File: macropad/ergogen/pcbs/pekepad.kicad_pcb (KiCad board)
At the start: 2 copper layers, 196 x 43.9 mm, 37 parts

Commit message: More case fixes
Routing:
- net P024: track 0.00 -> 183.9 mm, vias 0 -> 2
- net P008: track 0.00 -> 102.9 mm, vias 0 -> 1
- net P031: track 0.00 -> 101.5 mm, vias 0 -> 2
- net P106: track 0.00 -> 86.1 mm
- net P111: track 0.00 -> 85.7 mm
- net P022: track 0.00 -> 82.1 mm, vias 0 -> 2
- net P104: track 0.00 -> 81.7 mm
- net P009: track 0.00 -> 81.1 mm
- net P115: track 0.00 -> 71.9 mm, vias 0 -> 2
- net P113: track 0.00 -> 68.1 mm
- net P017: track 0.00 -> 66.6 mm, vias 0 -> 1
- net P100: track 0.00 -> 64.4 mm
- net P020: track 0.00 -> 52.7 mm, vias 0 -> 1
- net P029: track 0.00 -> 52.1 mm, vias 0 -> 1
- net P006: track 0.00 -> 44.7 mm
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
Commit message: More fixes to the case/pcb/plate
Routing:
- net P024: track 183.9 -> 0.00 mm, vias 2 -> 0
- net P008: track 102.9 -> 0.00 mm, vias 1 -> 0
- net P031: track 101.5 -> 0.00 mm, vias 2 -> 0
- net P106: track 86.1 -> 0.00 mm
- net P111: track 85.7 -> 0.00 mm
- net P022: track 82.1 -> 0.00 mm, vias 2 -> 0
- net P104: track 81.7 -> 0.00 mm
- net P009: track 81.1 -> 0.00 mm
- net P115: track 71.9 -> 0.00 mm, vias 2 -> 0
- net P113: track 68.1 -> 0.00 mm
- net P017: track 66.6 -> 0.00 mm, vias 1 -> 0
- net P100: track 64.4 -> 0.00 mm
- net P020: track 52.7 -> 0.00 mm, vias 1 -> 0
- net P029: track 52.1 -> 0.00 mm, vias 1 -> 0
- net P006: track 44.7 -> 0.00 mm
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
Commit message: forgot pcb wiring
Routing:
- net P024: track 0.00 -> 179.0 mm, vias 0 -> 2
- net P031: track 0.00 -> 103.2 mm, vias 0 -> 1
- net P008: track 0.00 -> 101.0 mm, vias 0 -> 1
- net P106: track 0.00 -> 86.1 mm
- net P111: track 0.00 -> 85.6 mm
- net P104: track 0.00 -> 81.7 mm
- net P009: track 0.00 -> 81.1 mm
- net P115: track 0.00 -> 73.6 mm, vias 0 -> 3
- net P113: track 0.00 -> 68.1 mm
- net P017: track 0.00 -> 66.6 mm, vias 0 -> 1
- net P100: track 0.00 -> 64.1 mm
- net P022: track 0.00 -> 59.7 mm, vias 0 -> 2
- net P029: track 0.00 -> 51.9 mm, vias 0 -> 1
- net P020: track 0.00 -> 46.8 mm, vias 0 -> 2
- net P006: track 0.00 -> 44.7 mm
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
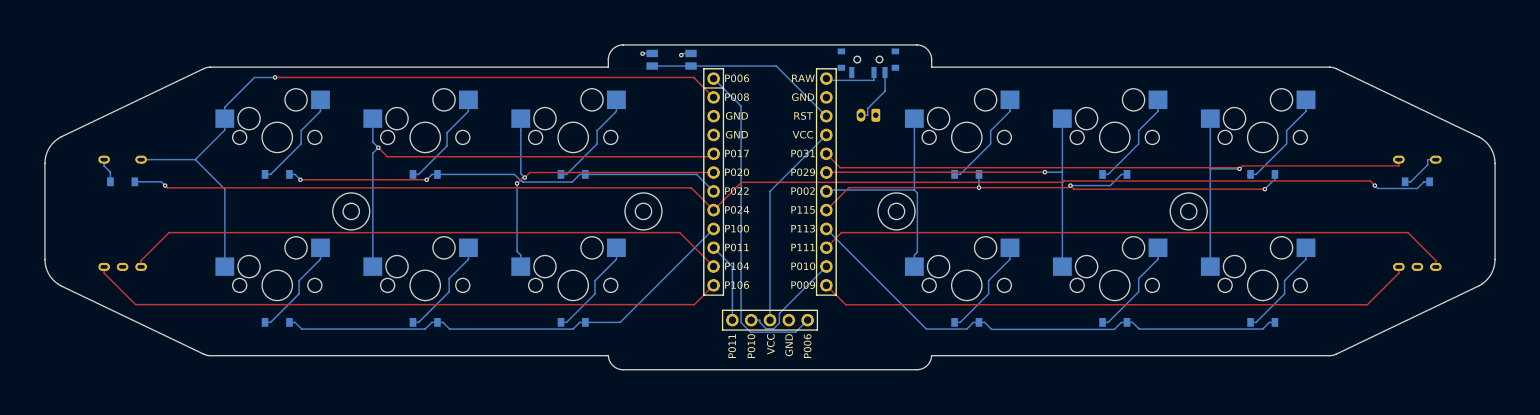
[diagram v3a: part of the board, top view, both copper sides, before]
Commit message: adjusting I2C/SPI pins
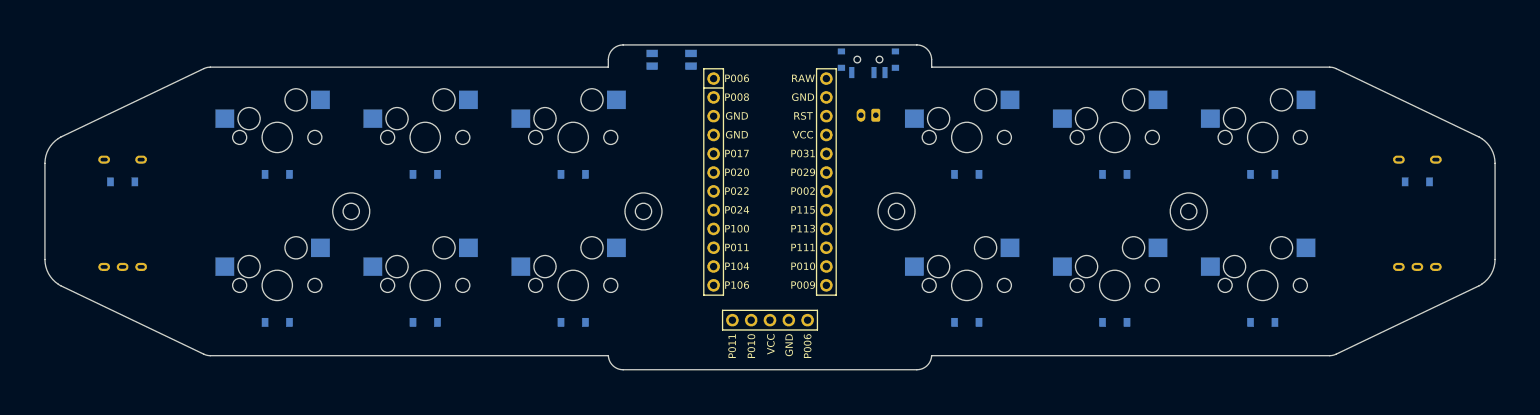
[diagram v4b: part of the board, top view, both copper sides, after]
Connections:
- D1 pad 1: P100 -> P011
- D13 pad 1: P024 -> P009
- D14 pad 1: P024 -> P009
- D2 pad 1: P022 -> P100
- D3 pad 1: P100 -> P011
- D4 pad 1: P022 -> P100
- D5 pad 1: P100 -> P011
- D6 pad 1: P022 -> P100
- RE2 pad C: P009 -> P010
- S3 pad 1: P017 -> P022
- S4 pad 1: P017 -> P022
- S5 pad 1: P020 -> P024
- S6 pad 1: P020 -> P024
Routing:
- net P024: track 179.0 -> 0.00 mm, vias 2 -> 0
- net P031: track 103.2 -> 0.00 mm, vias 1 -> 0
- net P008: track 101.0 -> 0.00 mm, vias 1 -> 0
- net P106: track 86.1 -> 0.00 mm
- net P111: track 85.6 -> 0.00 mm
- net P104: track 81.7 -> 0.00 mm
- net P009: track 81.1 -> 0.00 mm
- net P115: track 73.6 -> 0.00 mm, vias 3 -> 0
- net P113: track 68.1 -> 0.00 mm
- net P017: track 66.6 -> 0.00 mm, vias 1 -> 0
- net P100: track 64.1 -> 0.00 mm
- net P022: track 59.7 -> 0.00 mm, vias 2 -> 0
- net P029: track 51.9 -> 0.00 mm, vias 1 -> 0
- net P020: track 46.8 -> 0.00 mm, vias 2 -> 0
- net P006: track 44.7 -> 0.00 mm
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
